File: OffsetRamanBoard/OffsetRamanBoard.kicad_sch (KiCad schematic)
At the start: 1 part, among them U1 Teensy4.1_DEV-16771

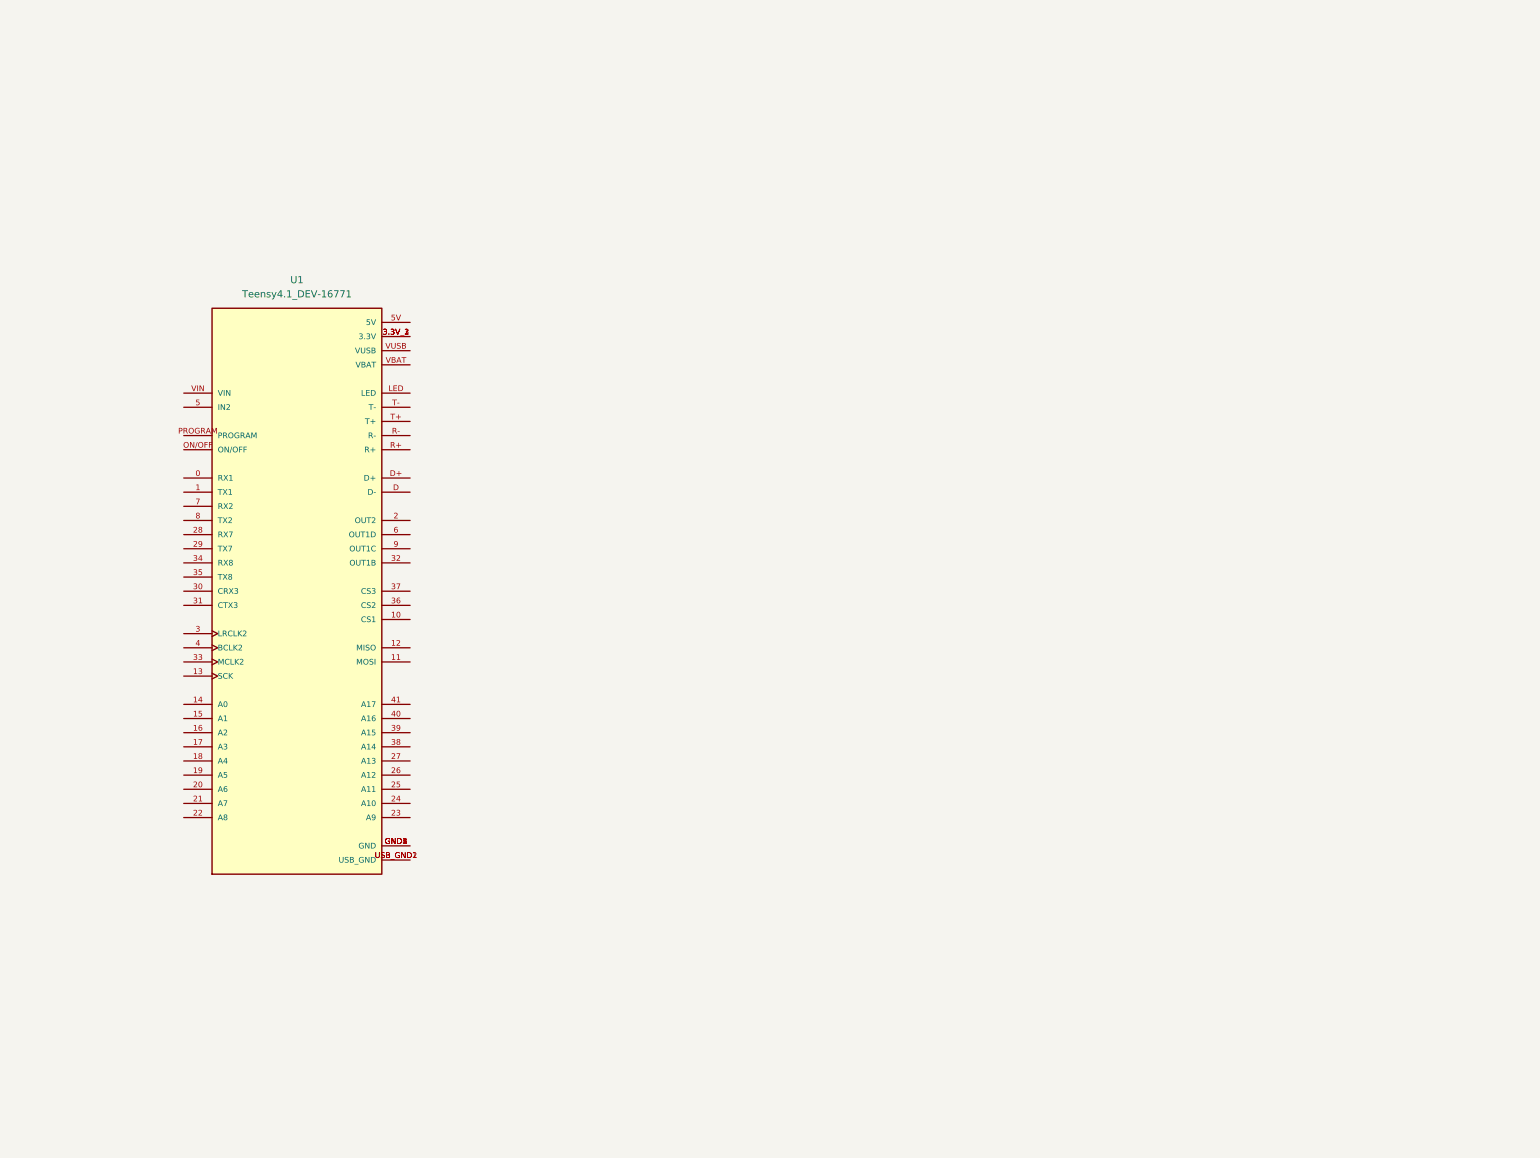
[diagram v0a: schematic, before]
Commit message: Update OffsetRamanBoard.kicad_sch
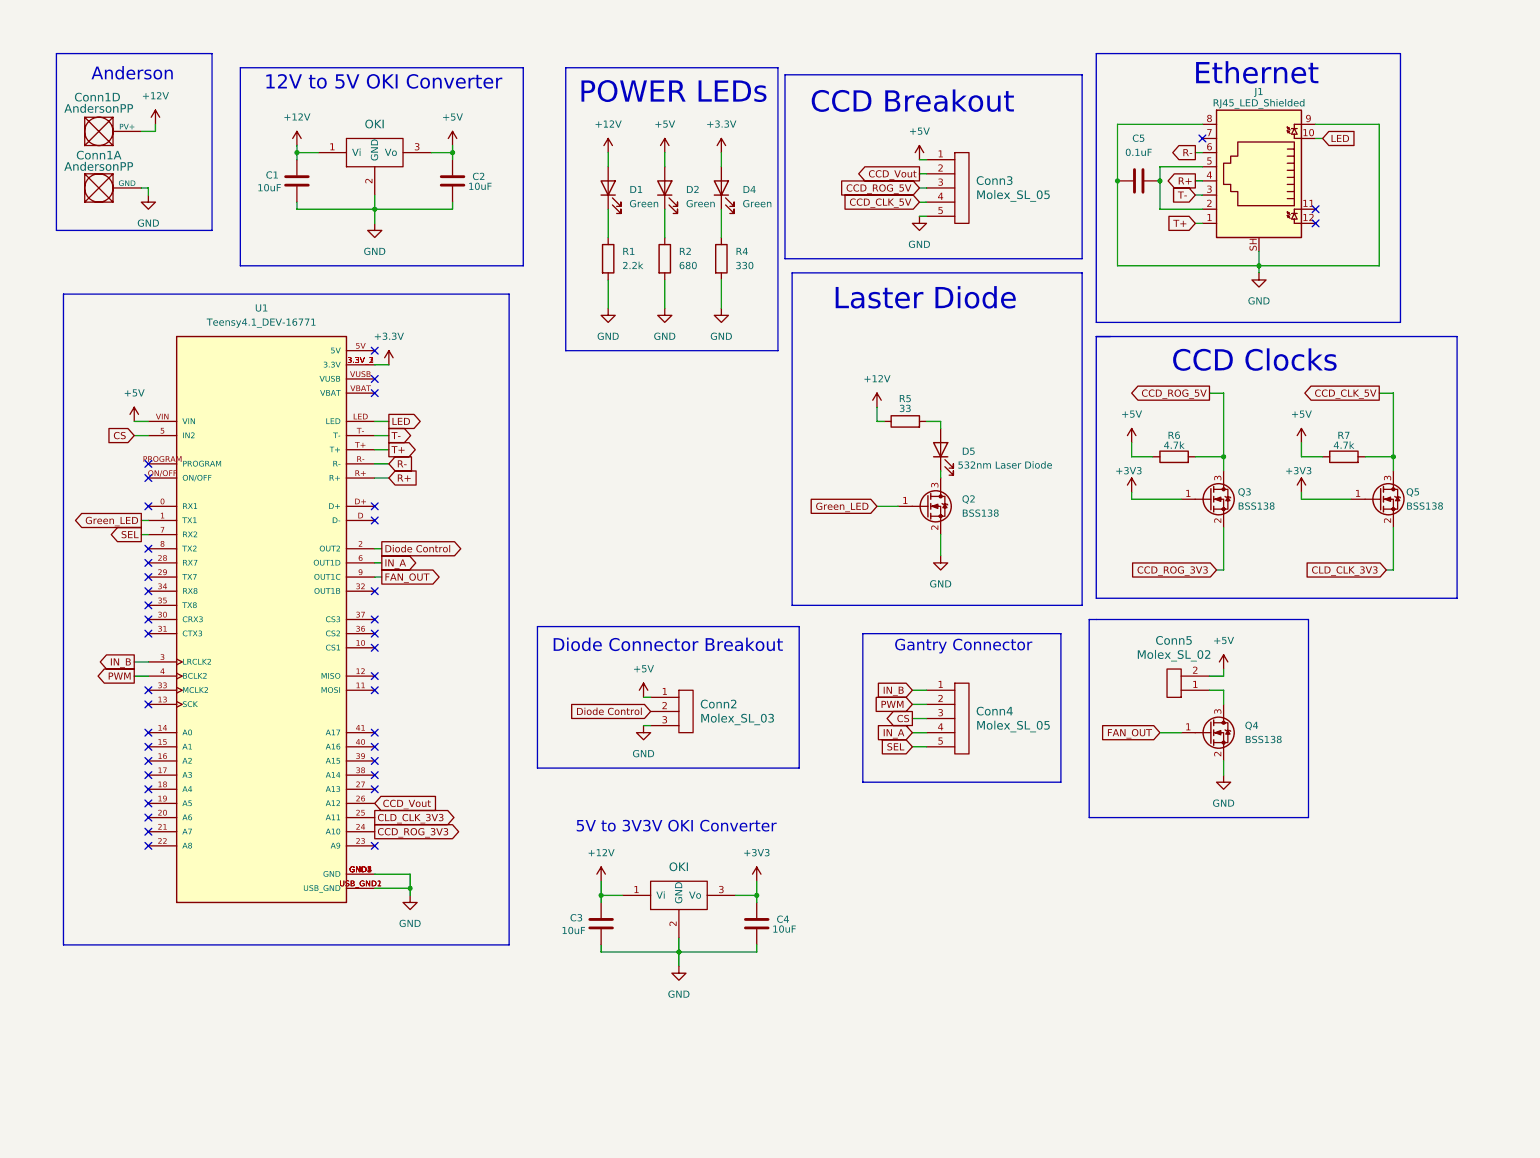
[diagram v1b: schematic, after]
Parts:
- added C1, C2, C3, C4: 10uF, Capacitor_SMD:C_0603_1608Metric_Pad1.08x0.95mm_HandSolder, symbol Device:C
- added C5: 0.1uF, Capacitor_SMD:C_0603_1608Metric_Pad1.08x0.95mm_HandSolder, symbol Device:C
- added Conn1: AndersonPP, MRDT_Connectors:Square_Anderson_2_H_Side_By_Side_PV, symbol MRDT_Connectors:AndersonPP
- added Conn2: Molex_SL_03, MRDT_Connectors:MOLEX_SL_03_Vertical, symbol MRDT_Connectors:Molex_SL_03
- added Conn3, Conn4: Molex_SL_05, MRDT_Connectors:MOLEX_SL_05_Vertical, symbol MRDT_Connectors:Molex_SL_05
- added Conn5: Molex_SL_02, MRDT_Connectors:MOLEX_SL_02_Vertical, symbol MRDT_Connectors:Molex_SL_02
- added D1, D2, D4: Green, LED_SMD:LED_0603_1608Metric_Pad1.05x0.95mm_HandSolder, symbol Device:LED
- added D5: 532nm Laser Diode, symbol Device:LED
- added J1: RJ45_LED_Shielded, MRDT_Connectors:RJ45_Teensy, symbol Connector:RJ45_LED_Shielded
- added Q2, Q3, Q4, Q5: BSS138, Package_TO_SOT_SMD:SOT-23, symbol Transistor_FET:BSS138
- added R1: 2.2k, Resistor_SMD:R_0603_1608Metric_Pad0.98x0.95mm_HandSolder, symbol Device:R
- added R2: 680, Resistor_SMD:R_0603_1608Metric_Pad0.98x0.95mm_HandSolder, symbol Device:R
- added R4: 330, Resistor_SMD:R_0603_1608Metric_Pad0.98x0.95mm_HandSolder, symbol Device:R
- added R5: 33, Resistor_SMD:R_0603_1608Metric_Pad0.98x0.95mm_HandSolder, symbol Device:R
- added R6, R7: 4.7k, Resistor_SMD:R_0603_1608Metric_Pad0.98x0.95mm_HandSolder, symbol Device:R
- added U3, U4: OKI, MRDT_Devices:OKI_Horizontal, symbol MRDT_Devices:OKI
- U1: footprint MODULE_DEV-16771 -> MRDT_Shields:Teensy_4_1_Ethernet
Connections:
- net Green_LED: now reaches U1.1 (TX1)
- net Green_LED: now also Q2.1 (G)
- net Diode Control: now reaches U1.2 (OUT2)
- net Diode Control: now also Conn2.2
- net CCD_ROG_3V3: now reaches U1.24 (A10)
- net CCD_ROG_3V3: now also Q3.2 (S)
- net CLD_CLK_3V3: now reaches U1.25 (A11)
- net CLD_CLK_3V3: now also Q5.2 (S)
- net CCD_Vout: now reaches U1.26 (A12)
- net CCD_Vout: now also Conn3.2
- net IN_B: now reaches U1.3 (LRCLK2)
- net IN_B: now also Conn4.1
- net +3.3V: now reaches U1.3.3V_1 (3.3V), U1.3.3V_2 (3.3V), U1.3.3V_3 (3.3V)
- net +3.3V: now also D4.2 (A)
- net PWM: now reaches U1.4 (BCLK2)
- net PWM: now also Conn4.2
- net CS: now reaches U1.5 (IN2)
- net CS: now also Conn4.3
- net IN_A: now reaches U1.6 (OUT1D)
- net IN_A: now also Conn4.4
- net SEL: now reaches U1.7 (RX2)
- net SEL: now also Conn4.5
- net FAN_OUT: now reaches U1.9 (OUT1C)
- net FAN_OUT: now also Q4.1 (G)
- net GND: now reaches U1.GND1 (GND), U1.GND2 (GND), U1.GND3 (GND), U1.GND4 (GND), U1.GND5 (GND)
- net GND: now also U1.USB_GND1 (USB_GND), U1.USB_GND2 (USB_GND), C1.2, C2.2, C3.2, C4.2, C5.2, Conn1.1 (GND), Conn2.3, Conn3.5, J1.8, J1.9, J1.SH, Q2.2 (S), Q4.2 (S), R1.2, R2.2, R4.2, U3.2 (GND), U4.2 (GND)
- net LED: now reaches U1.LED
- net LED: now also J1.10
- net R+: now reaches U1.R+
- net R+: now also J1.4
- net R-: now reaches U1.R-
- net R-: now also J1.6
- net T+: now reaches U1.T+
- net T+: now also J1.1
- net T-: now reaches U1.T-
- net T-: now also J1.3
- net +5V: now reaches U1.VIN
- net +5V: now also C2.1, Conn2.1, Conn3.1, Conn5.2, D2.2 (A), R6.1, R7.1, U3.3 (Vo)
- new net: D5.2 (A), R5.2
- new net: D1.1 (K), R1.1
- new net: D4.1 (K), R4.1
- new net: D5.1 (K), Q2.3 (D)
- new net: Conn5.1, Q4.3 (D)
- new net: C5.1, J1.2, J1.5
- new net: D2.1 (K), R2.1
- new net +12V: C1.1, C3.1, Conn1.4 (PV+), D1.2 (A), R5.1, U3.1 (Vi), U4.1 (Vi)
- new net +3V3: C4.1, Q3.1 (G), Q5.1 (G), U4.3 (Vo)
- new net CCD_CLK_5V: Conn3.4, Q5.3 (D), R7.2
- new net CCD_ROG_5V: Conn3.3, Q3.3 (D), R6.2
- no-connect marks 0 -> 41
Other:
- note added: "12V to 5V OKI Converter"
- note added: "5V to 3V3V OKI Converter"
- note added: "Anderson"
- note added: "CCD Breakout"
- note added: "CCD Clocks"
- note added: "Diode Connector Breakout"
- note added: "Ethernet"
- note added: "Gantry Connector"
- note added: "Laster Diode"
- note added: "POWER LEDs"

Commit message: Update OffsetRamanBoard.kicad_sch
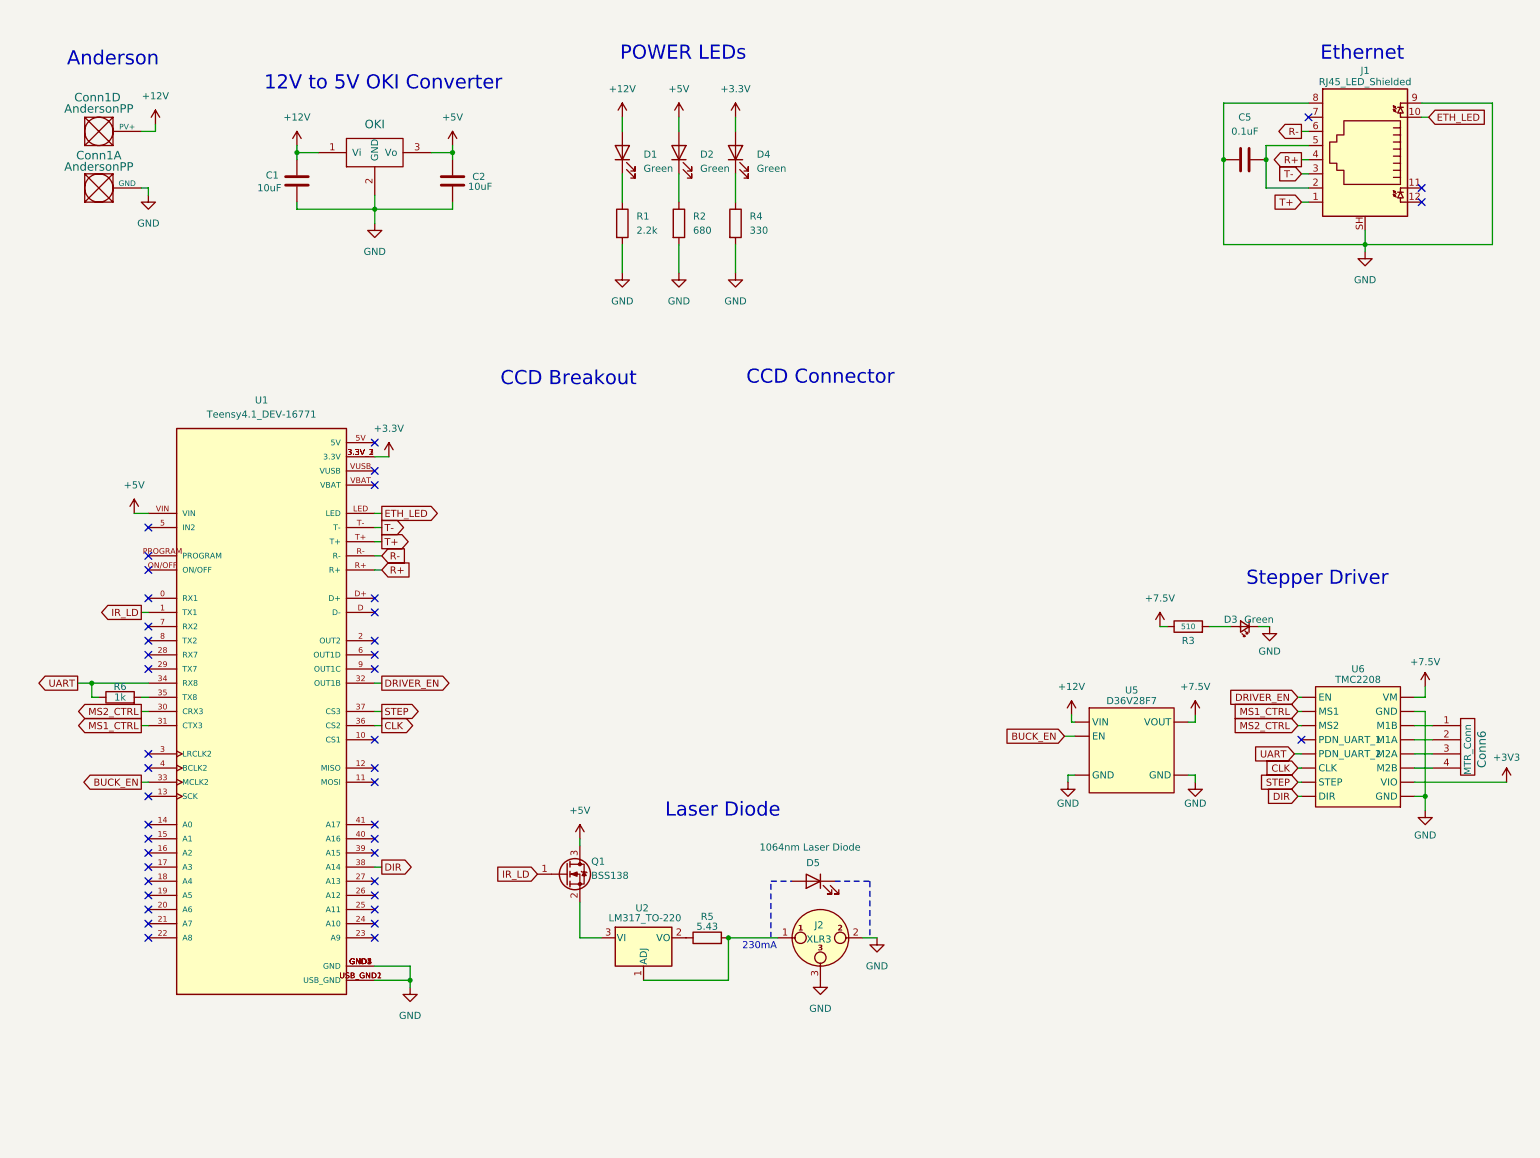
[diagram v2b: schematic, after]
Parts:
- removed C3, C4: 10uF, Capacitor_SMD:C_0603_1608Metric_Pad1.08x0.95mm_HandSolder, symbol Device:C
- removed Conn2: Molex_SL_03, MRDT_Connectors:MOLEX_SL_03_Vertical, symbol MRDT_Connectors:Molex_SL_03
- removed Conn3, Conn4: Molex_SL_05, MRDT_Connectors:MOLEX_SL_05_Vertical, symbol MRDT_Connectors:Molex_SL_05
- removed Conn5: Molex_SL_02, MRDT_Connectors:MOLEX_SL_02_Vertical, symbol MRDT_Connectors:Molex_SL_02
- removed Q2, Q3, Q4, Q5: BSS138, Package_TO_SOT_SMD:SOT-23, symbol Transistor_FET:BSS138
- removed R7: 4.7k, Resistor_SMD:R_0603_1608Metric_Pad0.98x0.95mm_HandSolder, symbol Device:R
- removed U4: OKI, MRDT_Devices:OKI_Horizontal, symbol MRDT_Devices:OKI
- added Conn6: MTR_Conn, MRDT_Connectors:MOLEX_SL_04_Vertical, symbol MRDT_Connectors:Molex_SL_04
- added D3: Green, LED_SMD:LED_0603_1608Metric_Pad1.05x0.95mm_HandSolder, symbol Device:LED_Small
- added J2: XLR3, symbol Connector_Audio:XLR3
- added Q1: BSS138, Package_TO_SOT_SMD:SOT-23, symbol Transistor_FET:BSS138
- added R3: 510, Resistor_SMD:R_0603_1608Metric_Pad0.98x0.95mm_HandSolder, symbol Device:R
- added U2: LM317_TO-220, Package_TO_SOT_THT:TO-220-3_Vertical, symbol Regulator_Linear:LM317_TO-220
- added U5: D36V28F7, FTIR_Footprints:D36V28F7_Buck, symbol Stepper_Driver_Headers:Pololu_7v5_Stepdown
- added U6: TMC2208, FTIR_Footprints:MODULE_TMC2208_SILENTSTEPSTICK, symbol Stepper_Driver_Headers:TMC2208_Breakout
- D5: value 532nm Laser Diode -> 1064nm Laser Diode
- R5: value 33 -> 5.43
- R6: value 4.7k -> 1k
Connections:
- net CCD_ROG_5V is gone; now on an unnamed net: R6.2
- net +12V: now also U5.VIN; no longer R5.1
- net +3V3: now also U6.VIO
- net +5V: now also Q1.3 (D); no longer R6.1
- net GND: now also D3.1 (K), J2.2, J2.3, U5.GND, U6.GND
- net at D5.2 (A): no longer R5.2
- net MS2_CTRL: now reaches U1.30 (CRX3)
- net MS2_CTRL: now also U6.MS2
- net MS1_CTRL: now reaches U1.31 (CTX3)
- net MS1_CTRL: now also U6.MS1
- net DRIVER_EN: now reaches U1.32 (OUT1B)
- net DRIVER_EN: now also U6.EN
- net BUCK_EN: now reaches U1.33 (MCLK2)
- net BUCK_EN: now also U5.EN
- net UART: now reaches U1.34 (RX8)
- net UART: now also R6.1, U6.PDN_UART_2
- net CLK: now reaches U1.36 (CS2)
- net CLK: now also U6.CLK
- net STEP: now reaches U1.37 (CS3)
- net STEP: now also U6.STEP
- net DIR: now reaches U1.38 (A14)
- net DIR: now also U6.DIR
- net CCD_ROG_3V3: no longer names the net of U1.24 (A10)
- net CCD_Vout: no longer names the net of U1.26 (A12)
- net CLD_CLK_3V3: no longer names the net of U1.25 (A11)
- net CS: no longer names the net of U1.5 (IN2)
- net Diode Control: no longer names the net of U1.2 (OUT2)
- net FAN_OUT: no longer names the net of U1.9 (OUT1C)
- net Green_LED renamed IR_LD
- net IR_LD: now also Q1.1 (G)
- net IN_A: no longer names the net of U1.6 (OUT1D)
- net IN_B: no longer names the net of U1.3 (LRCLK2)
- net LED renamed ETH_LED
- net PWM: no longer names the net of U1.4 (BCLK2)
- net SEL: no longer names the net of U1.7 (RX2)
- new net: D3.2 (A), R3.2
- new net: Conn6.1, U6.M1B
- new net: Conn6.2, U6.M1A
- new net: Conn6.3, U6.M2A
- new net: Conn6.4, U6.M2B
- new net: J2.1, R5.2, U2.1 (ADJ)
- new net: R5.1, U2.2 (VO)
- new net: Q1.2 (S), U2.3 (VI)
- new net +7.5V: R3.1, U5.VOUT, U6.VM
- no-connect marks 41 -> 43
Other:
- note added: "230mA"
- note added: "CCD Connector"
- note added: "Laser Diode"
- note added: "Stepper Driver"
- note removed: "5V to 3V3V OKI Converter"
- note removed: "CCD Clocks"
- note removed: "Diode Connector Breakout"
- note removed: "Gantry Connector"
- note removed: "Laster Diode"
- moved on the sheet: C5, D1, D2, D4, D5, J1, R1, R2, R4, U1

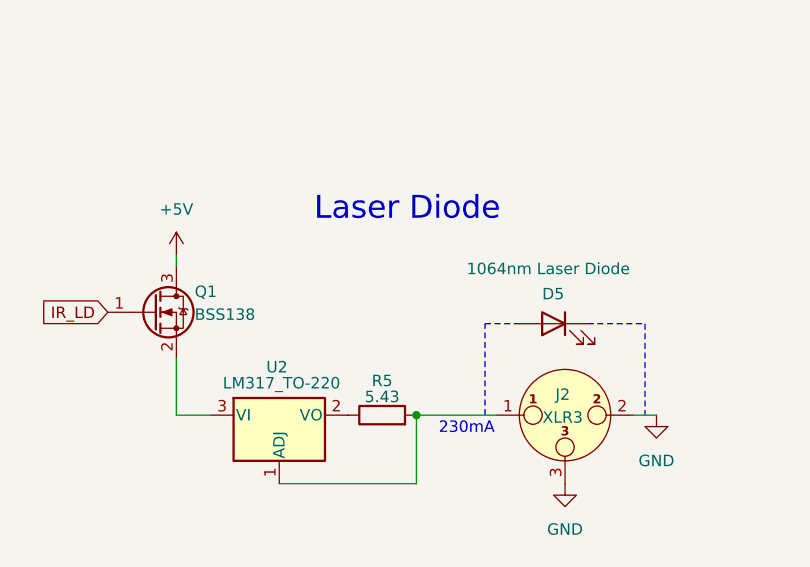
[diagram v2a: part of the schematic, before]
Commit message: Added mini xlr connector with datasheet
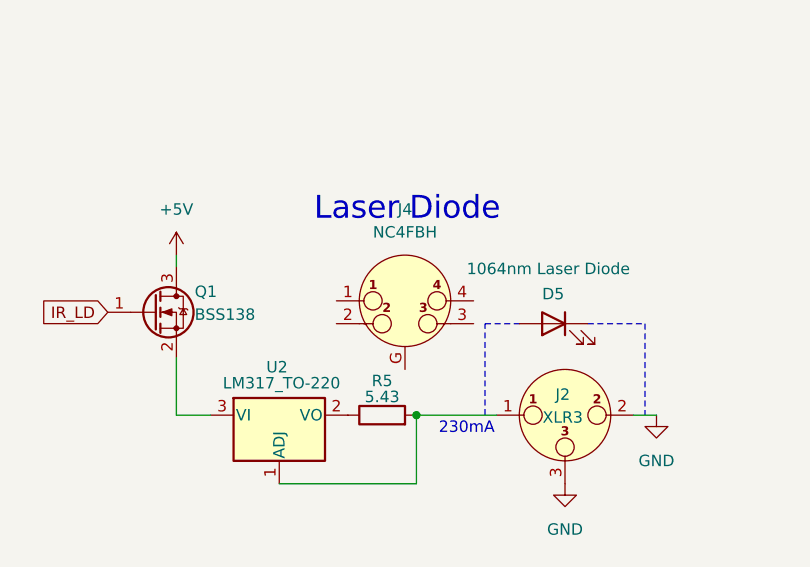
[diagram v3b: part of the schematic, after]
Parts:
- added J4: NC4FBH, Connector_Audio:Jack_XLR_Neutrik_NC4FBH_Horizontal, symbol Connector_Audio:NC4FBH
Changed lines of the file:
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@@
+	)
+	(symbol
+		(lib_id "Connector_Audio:NC4FBH")
+		(at 138.43 166.37 0)
+		(unit 1)
+		(exclude_from_sim no)
+		(in_bom yes)
+		(on_board yes)
+		(dnp no)
+		(fields_autoplaced yes)
+		(property "Reference" "J4"
+			(at 138.43 156.21 0)
+			(effects
+				(font
+					(size 1.27 1.27)
+				)
+			)
+		)
+		(property "Value" "NC4FBH"
+			(at 138.43 158.75 0)
+			(effects
+				(font
+					(size 1.27 1.27)
+				)
+			)
+		)
+		(property "Footprint" "Connector_Audio:Jack_XLR_Neutrik_NC4FBH_Horizontal"
+			(at 138.43 166.37 0)
+			(effects
+				(font
+					(size 1.27 1.27)
+				)
+				(hide yes)
+			)
+		)
+		(property "Datasheet" "https://www.mouser.com/ProductDetail/Amphenol-Audio/AG4MCCH?qs=t8%2F5FiDdxGb12fmfPDKMLg%3D%3D"
+			(at 138.43 166.37 0)
+			(effects
+				(font
+					(size 1.27 1.27)
+				)
+				(hide yes)
+			)
+		)
+		(property "Description" "B Series, 4 pole female XLR receptacle, grounding: separate ground contact to mating connector shell and front panel, horizontal PCB mount"
+			(at 138.43 166.37 0)
+			(effects
+				(font
+					(size 1.27 1.27)
+				)
+				(hide yes)
+			)
+		)
+		(pin "4"
+		)
+		(pin "1"
+		)
+		(pin "2"
+		)
+		(pin "G"
+		)
+		(pin "3"
+		)
+		(instances
+			(project ""
+				(path "/9ff4b029-9861-4feb-a35d-1121756e6981"
+					(reference "J4")
+					(unit 1)
+				)
+			)
+		)
 	)
 	(symbol
